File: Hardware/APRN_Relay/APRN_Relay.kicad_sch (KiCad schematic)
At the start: 41 parts, among them J101 SERVO1, J102 SERVO2, J103 PTT, J104 Pi_Zero, J105 RADIO, J106 CHG, J107 PWR, J108 BAT, U101 DHT11, U102 INA219AIDR, U103 NCV1117ST50T3G

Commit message: Remove power flag from input of current sensor
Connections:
- net BATTERY: no longer JP101.2 (B)
- net CHARGE: now also JP101.2 (B)
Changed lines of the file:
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@@
     (company "Kitsune Scientific")
-  )
-  (junction (at 234.95 102.87) (diameter 0) (color 0 0 0 0)
   )
   (junction (at 87.63 64.77) (diameter 0) (color 0 0 0 0)
@@
     (stroke (width 0) (type default) (color 0 0 0 0))
   )
-  (wire (pts (xy 234.95 102.87) (xy 236.22 102.87))
+  (wire (pts (xy 224.79 102.87) (xy 236.22 102.87))
     (stroke (width 0) (type default) (color 0 0 0 0))
   )
@@
   )
   (wire (pts (xy 224.79 88.9) (xy 224.79 97.79))
-    (stroke (width 0) (type default) (color 0 0 0 0))
-  )
-  (wire (pts (xy 224.79 102.87) (xy 234.95 102.87))
     (stroke (width 0) (type default) (color 0 0 0 0))
   )
@@
     (effects (font (size 1.27 1.27)) (justify left bottom))
   )
-  (label "BATTERY" (at 174.625 39.37 180)
-    (effects (font (size 1.27 1.27)) (justify right bottom))
-  )
   (label "SDA" (at 261.62 95.25 180)
     (effects (font (size 1.27 1.27)) (justify right bottom))
@@
   )
   (label "A0" (at 261.62 105.41 180)
+    (effects (font (size 1.27 1.27)) (justify right bottom))
+  )
+  (label "CHARGE" (at 174.625 39.37 180)
     (effects (font (size 1.27 1.27)) (justify right bottom))
   )
@@
     )
     (property "Datasheet" "" (id 3) (at 167.64 30.48 0)
-      (effects (font (size 1.27 1.27)) hide)
-    )
-    (pin "1")
-  )
-  (symbol (lib_id "power:PWR_FLAG") (at 234.95 102.87 0) (unit 1)
-    (in_bom yes) (on_board yes) (fields_autoplaced)
-    (property "Reference" "#FLG0105" (id 0) (at 234.95 100.965 0)
-      (effects (font (size 1.27 1.27)) hide)
-    )
-    (property "Value" "PWR_FLAG" (id 1) (at 234.95 97.79 0)
-      (effects (font (size 1.27 1.27)) hide)
-    )
-    (property "Footprint" "" (id 2) (at 234.95 102.87 0)
-      (effects (font (size 1.27 1.27)) hide)
-    )
-    (property "Datasheet" "~" (id 3) (at 234.95 102.87 0)
       (effects (font (size 1.27 1.27)) hide)
     )
@@
       (reference "#FLG0104") (unit 1) (value "PWR_FLAG") (footprint "")
     )
-    (path "/61c58c11-2766-4dd4-9607-4af59e4f7fa0"
-      (reference "#FLG0105") (unit 1) (value "PWR_FLAG") (footprint "")
-    )
     (path "/44289aa4-8cb7-4770-bd78-b7737550e23a"

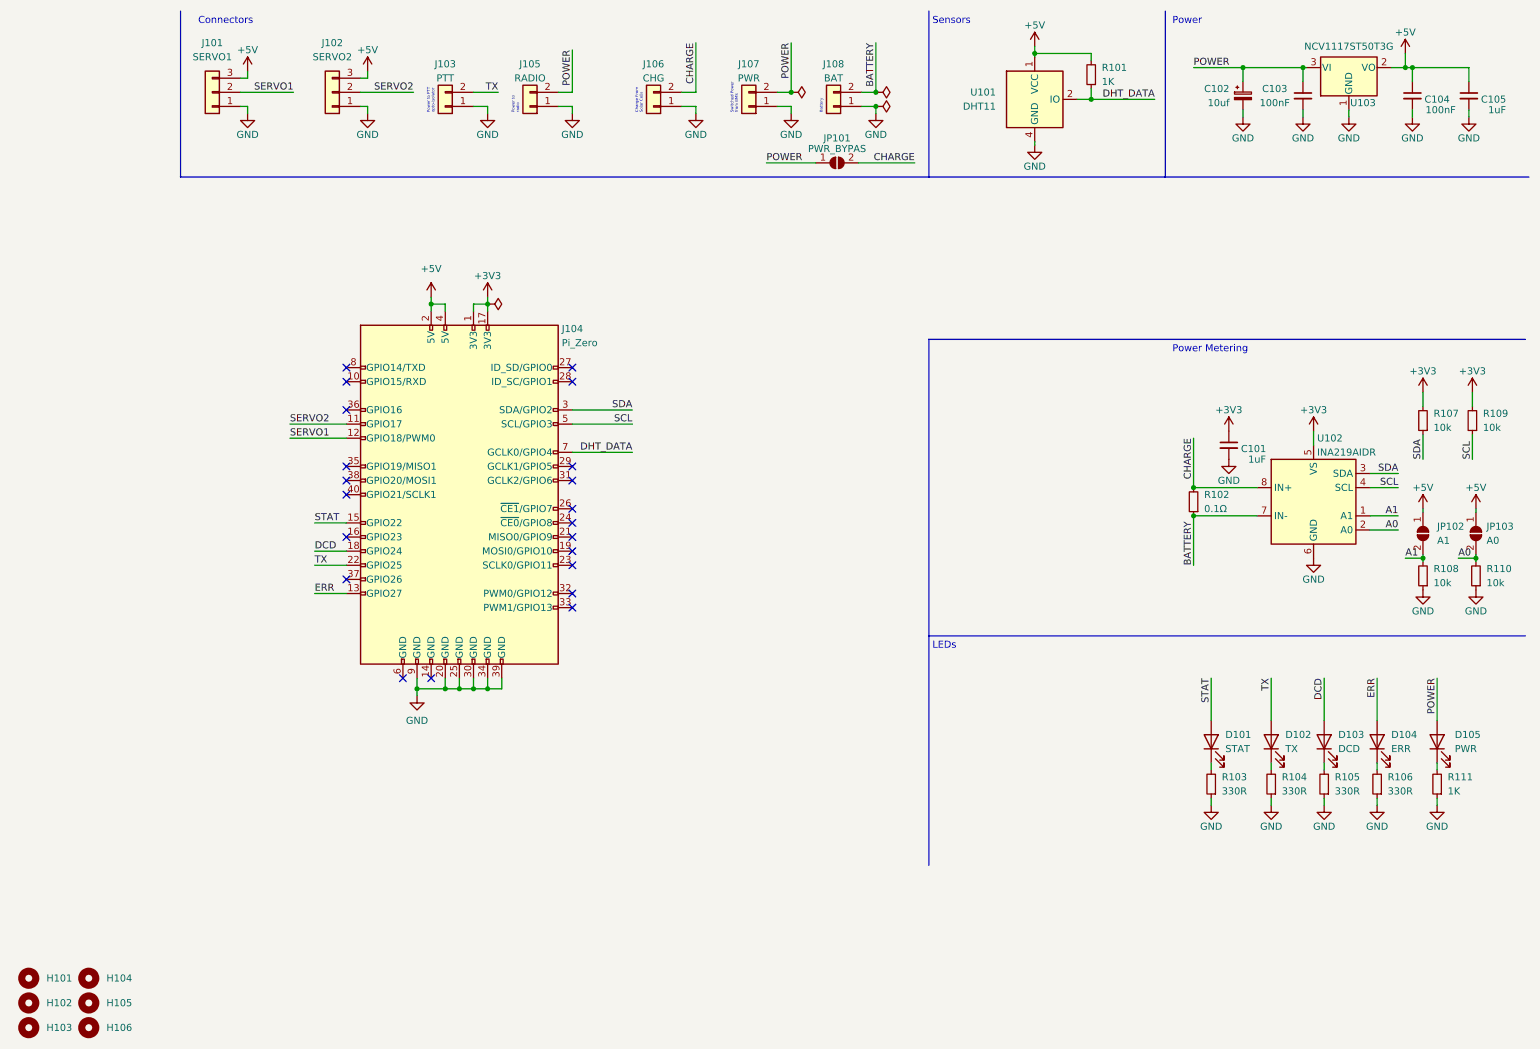
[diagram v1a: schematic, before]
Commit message: Add PTT DNP
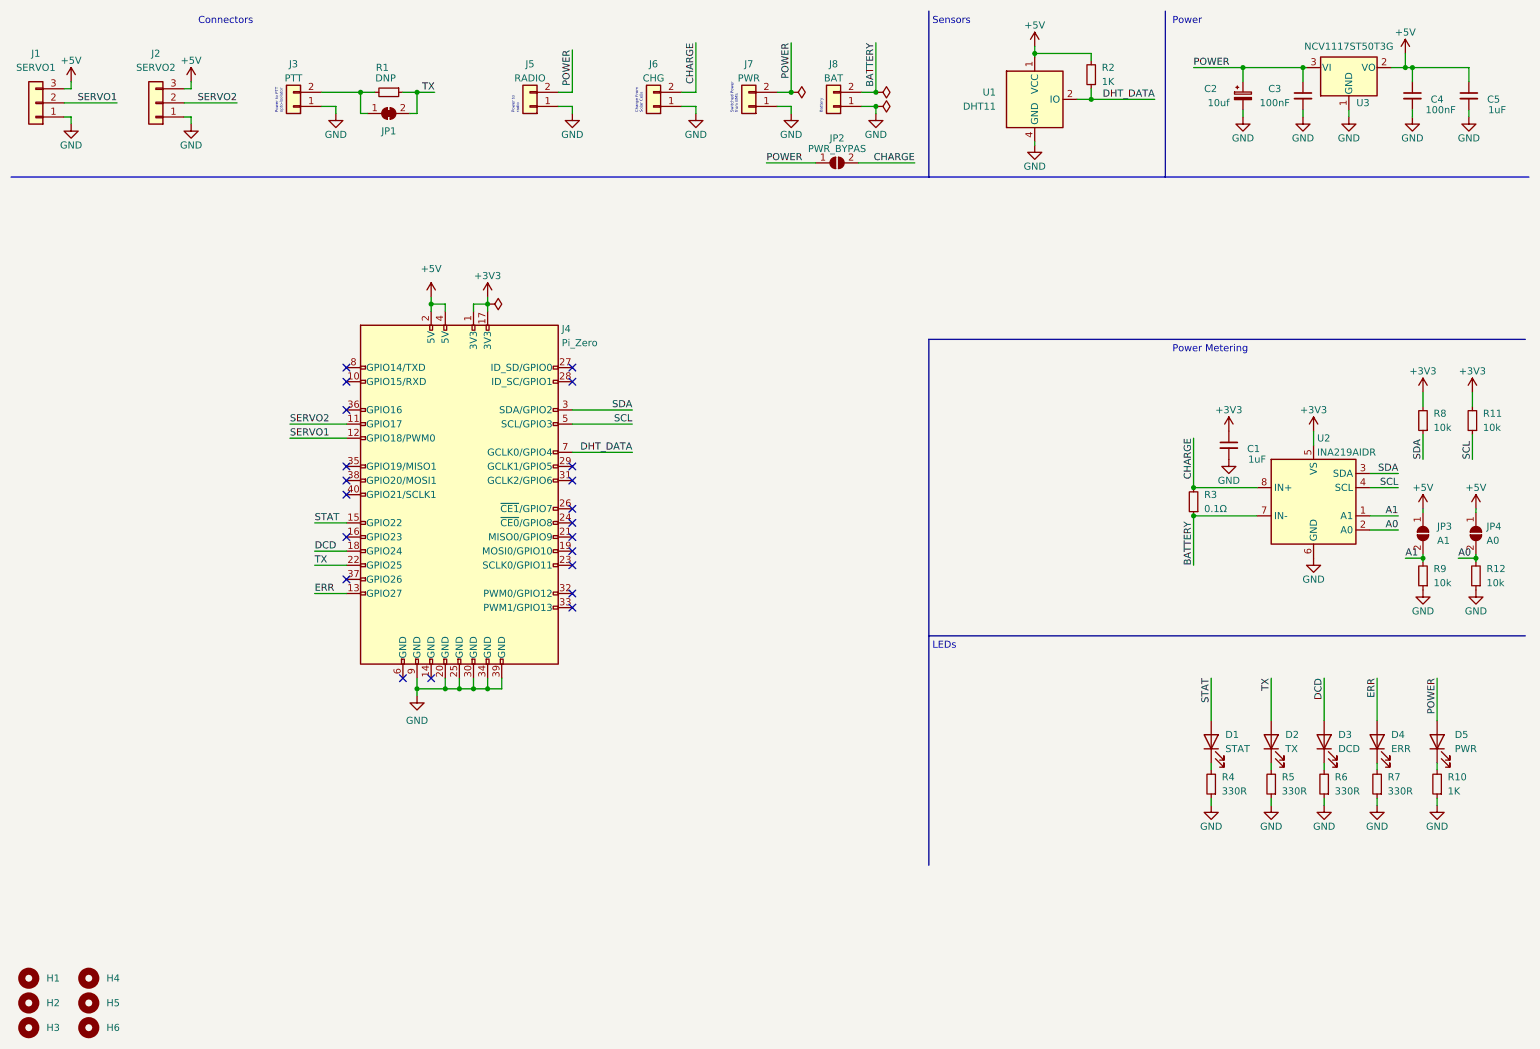
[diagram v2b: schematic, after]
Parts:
- added JP1: SolderJumper_2_Bridged, Jumper:SolderJumper-2_P1.3mm_Bridged_Pad1.0x1.5mm, symbol Jumper:SolderJumper_2_Bridged
- added R1: DNP, Resistor_SMD:R_0805_2012Metric, symbol Device:R_Small
- renumbered C101 to C1, C102 to C2, C103 to C3, C104 to C4, C105 to C5, D101 to D1, D102 to D2, D103 to D3, D104 to D4, D105 to D5, H101 to H1, H102 to H2, H103 to H3, H104 to H4, H105 to H5, H106 to H6, J101 to J1, J102 to J2, J103 to J3, J104 to J4, J105 to J5, J106 to J6, J107 to J7, J108 to J8, JP101 to JP2, JP102 to JP3, JP103 to JP4, R111 to R10, R109 to R11, R110 to R12, R101 to R2, R102 to R3, R103 to R4, R104 to R5, R105 to R6, R106 to R7, R107 to R8, R108 to R9, U101 to U1, U102 to U2, U103 to U3
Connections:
- net TX: now also JP1.2 (B), R1.1; no longer J3.2 (Pin_2)
- new net: J3.2 (Pin_2), JP1.1 (A), R1.2
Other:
- moved on the sheet: J1, J2, J3

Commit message: bump with new plugs on the back
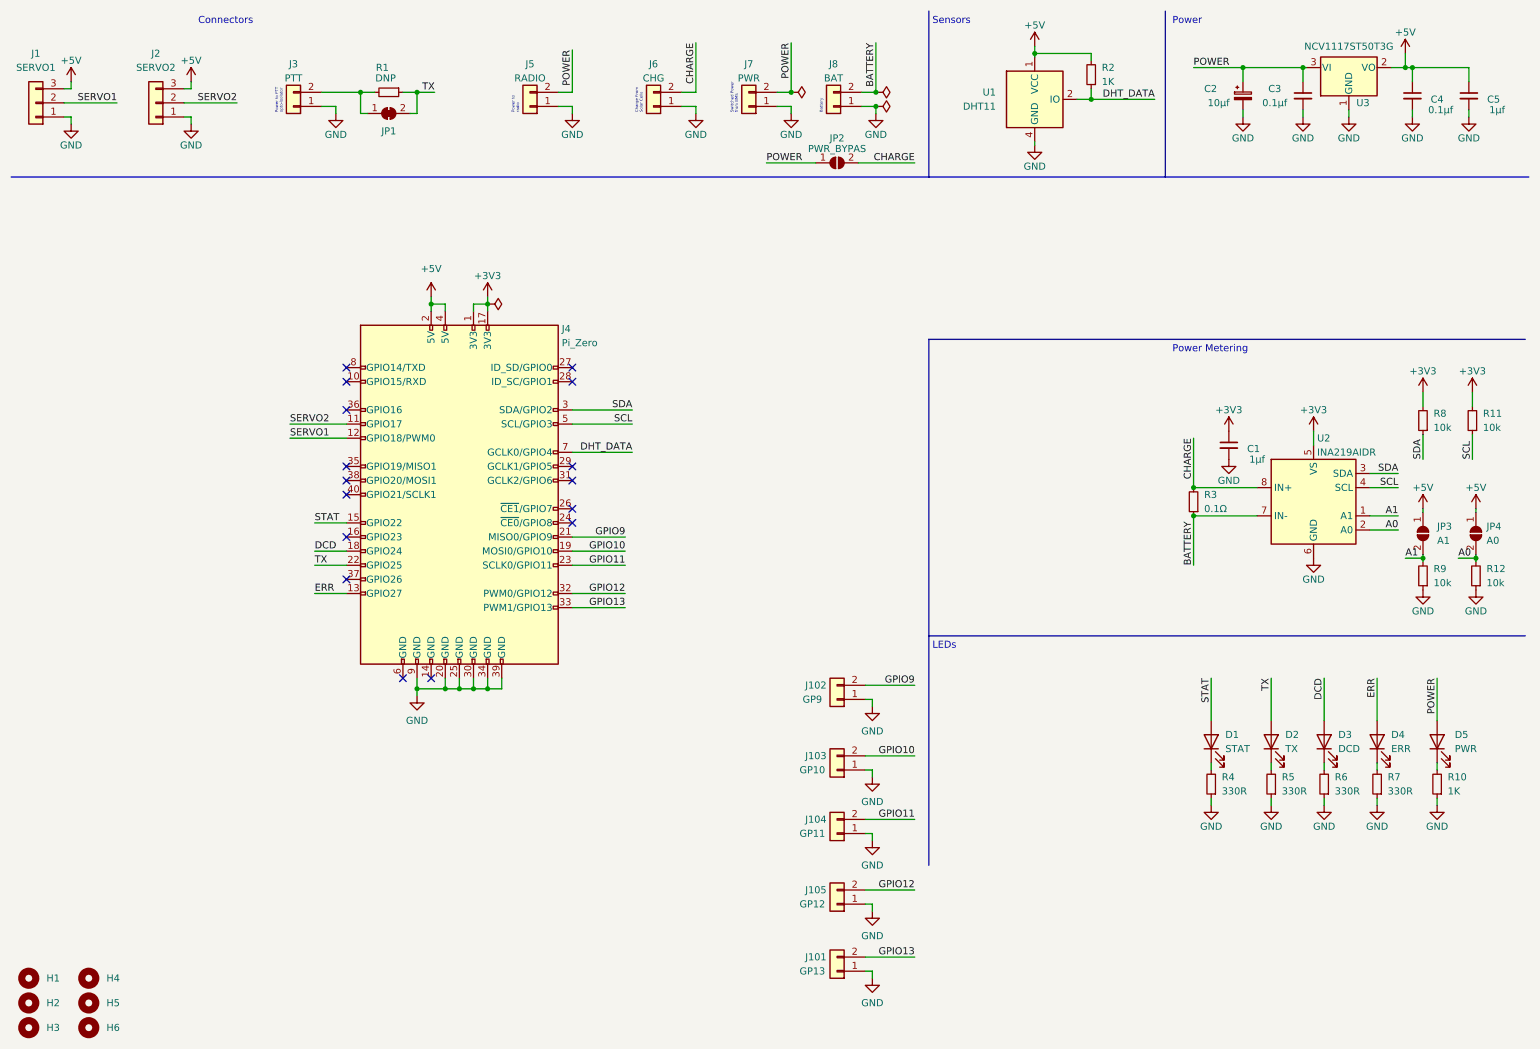
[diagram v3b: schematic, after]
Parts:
- added J101: GP13, Connector_JST:JST_EH_S2B-EH_1x02_P2.50mm_Horizontal, symbol Connector_Generic:Conn_01x02
- added J102: GP9, Connector_JST:JST_EH_S2B-EH_1x02_P2.50mm_Horizontal, symbol Connector_Generic:Conn_01x02
- added J103: GP10, Connector_JST:JST_EH_S2B-EH_1x02_P2.50mm_Horizontal, symbol Connector_Generic:Conn_01x02
- added J104: GP11, Connector_JST:JST_EH_S2B-EH_1x02_P2.50mm_Horizontal, symbol Connector_Generic:Conn_01x02
- added J105: GP12, Connector_JST:JST_EH_S2B-EH_1x02_P2.50mm_Horizontal, symbol Connector_Generic:Conn_01x02
- C1, C5: value 1uF -> 1μf
- C2: value 10uf -> 10μf
- C3, C4: value 100nF -> 0.1μf
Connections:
- net GND: now also J101.1 (Pin_1), J102.1 (Pin_1), J103.1 (Pin_1), J104.1 (Pin_1), J105.1 (Pin_1)
- net GPIO10: now reaches J4.19 (MOSI0/GPIO10)
- net GPIO10: now also J103.2 (Pin_2)
- net GPIO9: now reaches J4.21 (MISO0/GPIO9)
- net GPIO9: now also J102.2 (Pin_2)
- net GPIO11: now reaches J4.23 (SCLK0/GPIO11)
- net GPIO11: now also J104.2 (Pin_2)
- net GPIO12: now reaches J4.32 (PWM0/GPIO12)
- net GPIO12: now also J105.2 (Pin_2)
- net GPIO13: now reaches J4.33 (PWM1/GPIO13)
- net GPIO13: now also J101.2 (Pin_2)
- no-connect marks 21 -> 16

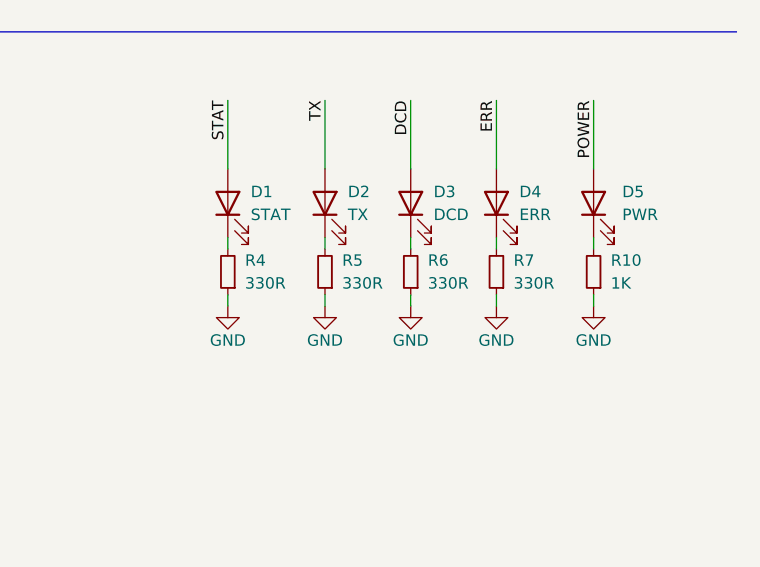
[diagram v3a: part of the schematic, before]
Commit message: Add 3d models
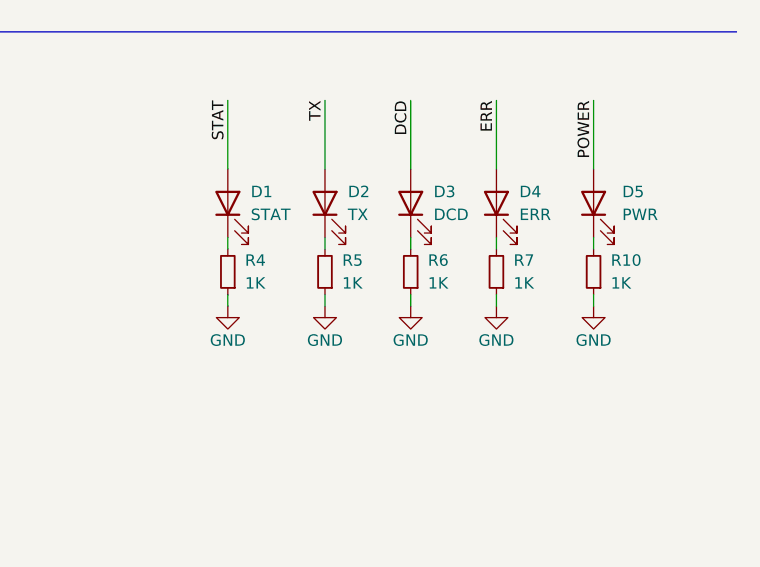
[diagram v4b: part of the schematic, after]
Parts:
- R4, R5, R6, R7: value 330R -> 1K
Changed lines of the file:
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@@
       (effects (font (size 1.27 1.27)) (justify right))
     )
-    (property "Value" "330R" (id 1) (at 229.87 152.4 0)
+    (property "Value" "1K" (id 1) (at 229.87 152.4 0)
       (effects (font (size 1.27 1.27)) (justify right))
     )
@@
       (effects (font (size 1.27 1.27)) (justify right))
     )
-    (property "Value" "330R" (id 1) (at 240.665 152.4 0)
+    (property "Value" "1K" (id 1) (at 240.665 152.4 0)
       (effects (font (size 1.27 1.27)) (justify right))
     )
@@
       (effects (font (size 1.27 1.27)) (justify right))
     )
-    (property "Value" "330R" (id 1) (at 250.19 152.4 0)
+    (property "Value" "1K" (id 1) (at 250.19 152.4 0)
       (effects (font (size 1.27 1.27)) (justify right))
     )
@@
       (effects (font (size 1.27 1.27)) (justify right))
     )
-    (property "Value" "330R" (id 1) (at 259.715 152.4 0)
+    (property "Value" "1K" (id 1) (at 259.715 152.4 0)
       (effects (font (size 1.27 1.27)) (justify right))
     )
@@
     )
     (path "/9d823249-29a5-4c29-9cd9-22157bae975d"
-      (reference "R4") (unit 1) (value "330R") (footprint "Resistor_SMD:R_0805_2012Metric")
+      (reference "R4") (unit 1) (value "1K") (footprint "Resistor_SMD:R_0805_2012Metric")
     )
     (path "/d06e768f-7379-46b4-bd72-628e1fe49db1"
-      (reference "R5") (unit 1) (value "330R") (footprint "Resistor_SMD:R_0805_2012Metric")
+      (reference "R5") (unit 1) (value "1K") (footprint "Resistor_SMD:R_0805_2012Metric")
     )
     (path "/d721cbd4-33b8-4a19-8a2c-59f63a9c828b"
-      (reference "R6") (unit 1) (value "330R") (footprint "Resistor_SMD:R_0805_2012Metric")
+      (reference "R6") (unit 1) (value "1K") (footprint "Resistor_SMD:R_0805_2012Metric")
     )
     (path "/e144cdc9-a107-4fe4-b253-f0c5ecd0cc6e"
-      (reference "R7") (unit 1) (value "330R") (footprint "Resistor_SMD:R_0805_2012Metric")
+      (reference "R7") (unit 1) (value "1K") (footprint "Resistor_SMD:R_0805_2012Metric")
     )
     (path "/7b6ac039-b8a6-4fc4-beab-efe1dfa45534"
